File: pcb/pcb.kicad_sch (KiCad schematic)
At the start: 52 parts

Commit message: err in sch
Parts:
- removed C? (x2): 100uF, symbol Device:C_Polarized_Small
- removed D? (x3): 1N5822, Diode_THT:D_DO-201AD_P15.24mm_Horizontal, symbol Diode:1N5822
- removed R? (x2): 10k, symbol Device:R_Small
- added C?: 4.7n, symbol Device:C_Small
- added Q1: AO3400A, Package_TO_SOT_SMD:SOT-23, symbol Transistor_FET:AO3400A
- added R11, R4: 100k, symbol Device:R_Small
- added R12, R13, R14: 85, symbol Device:R_Small
- added R3: 10k, symbol Device:R_Small
- L2: renamed from L?; value . -> 1.2uH
- L3: renamed from L?; value . -> 20uH
- R2: renamed from R?; value R -> 200k
- gave numbers to parts that had none: 42
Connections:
- net +12V: now also R11.2; no longer D4.1 (K), J2.2 (Pin_2), J2.3 (Pin_3), L2.1, Q2.3 (D), Q3.3 (D), Q4.3 (D)
- net +3V3: now also R4.2
- net GND: now also Q1.2 (S); no longer J2.4 (Pin_4), Q5.3 (S)
- net at U1.5 (PB0): now also R3.2
- net at Q5.1 (G): now also Q1.3 (D), R11.1
- net at R17.2, R18.1, U4.2 (REF): now also C?.1
- net at R16.2, U3.2, U4.1 (K): now also C?.2
- new net: Q3.3 (D), R13.1
- new net: J2.3 (Pin_3), R13.2
- new net: J2.2 (Pin_2), R12.2
- new net: J2.4 (Pin_4), R14.2
- new net: D4.1 (K), L2.1, Q5.3 (S)
- new net: Q2.3 (D), R12.1
- new net: Q4.3 (D), R14.1
- new net: Q1.1 (G), R3.1, R4.1
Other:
- moved on the sheet: C6, J2, Q2, Q3, Q4, Q5, R10, R15, R17, R18, R5, R6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

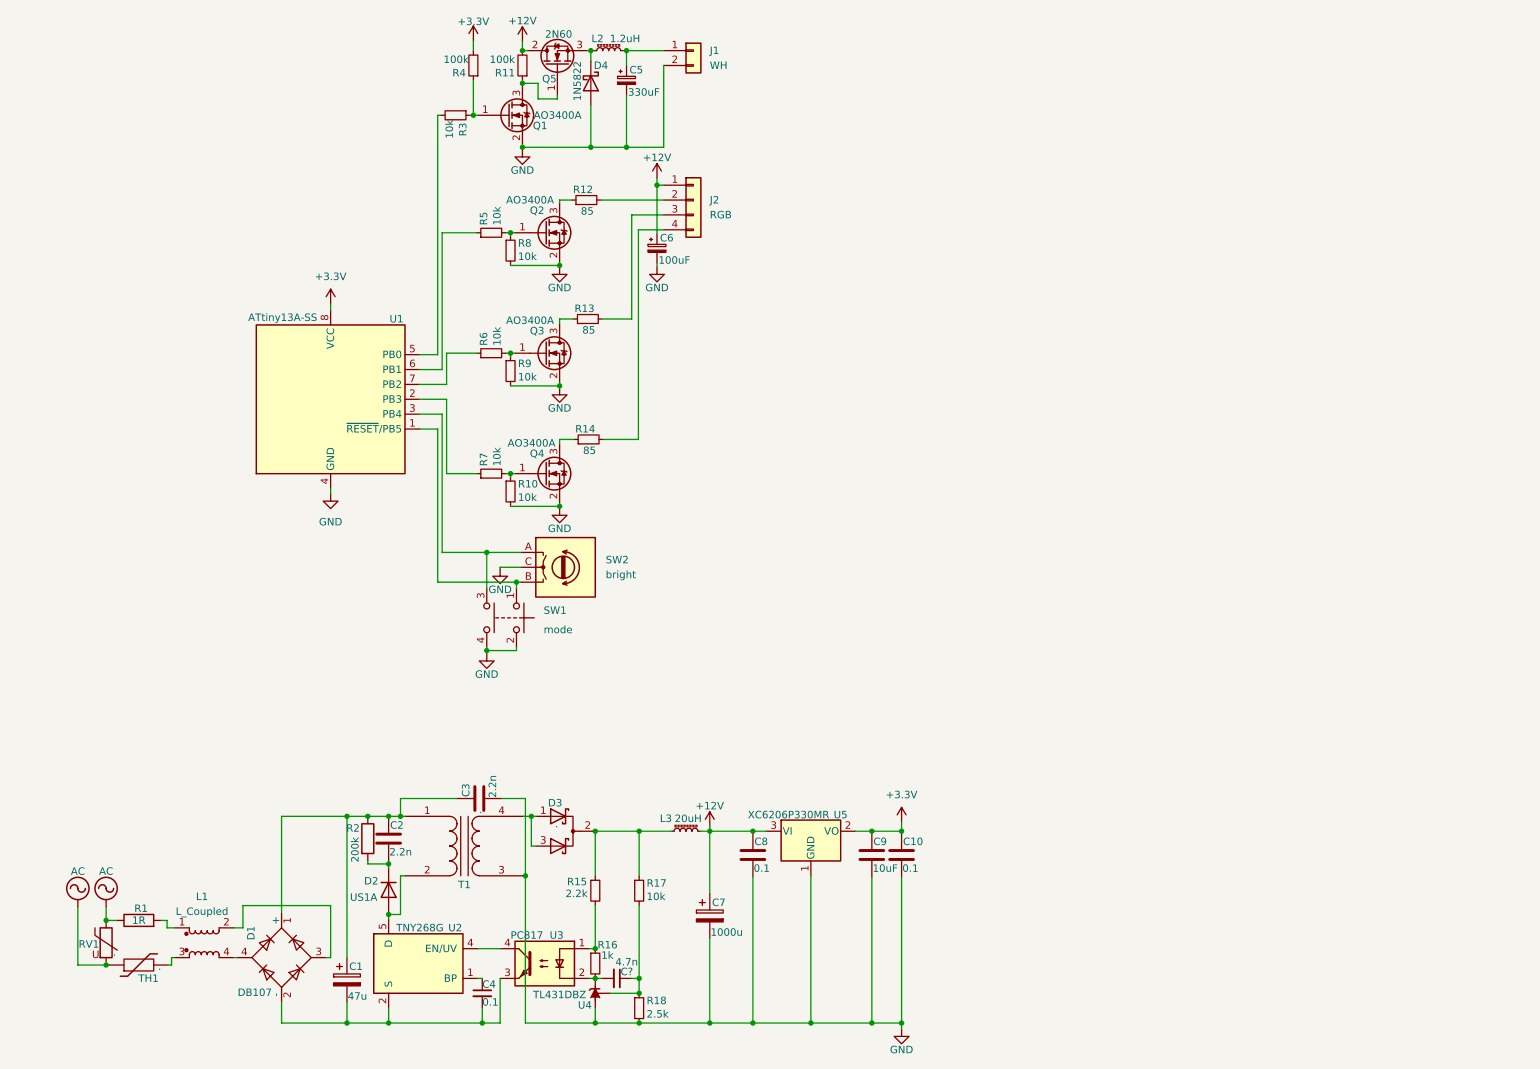
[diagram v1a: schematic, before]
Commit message: short circuit protection
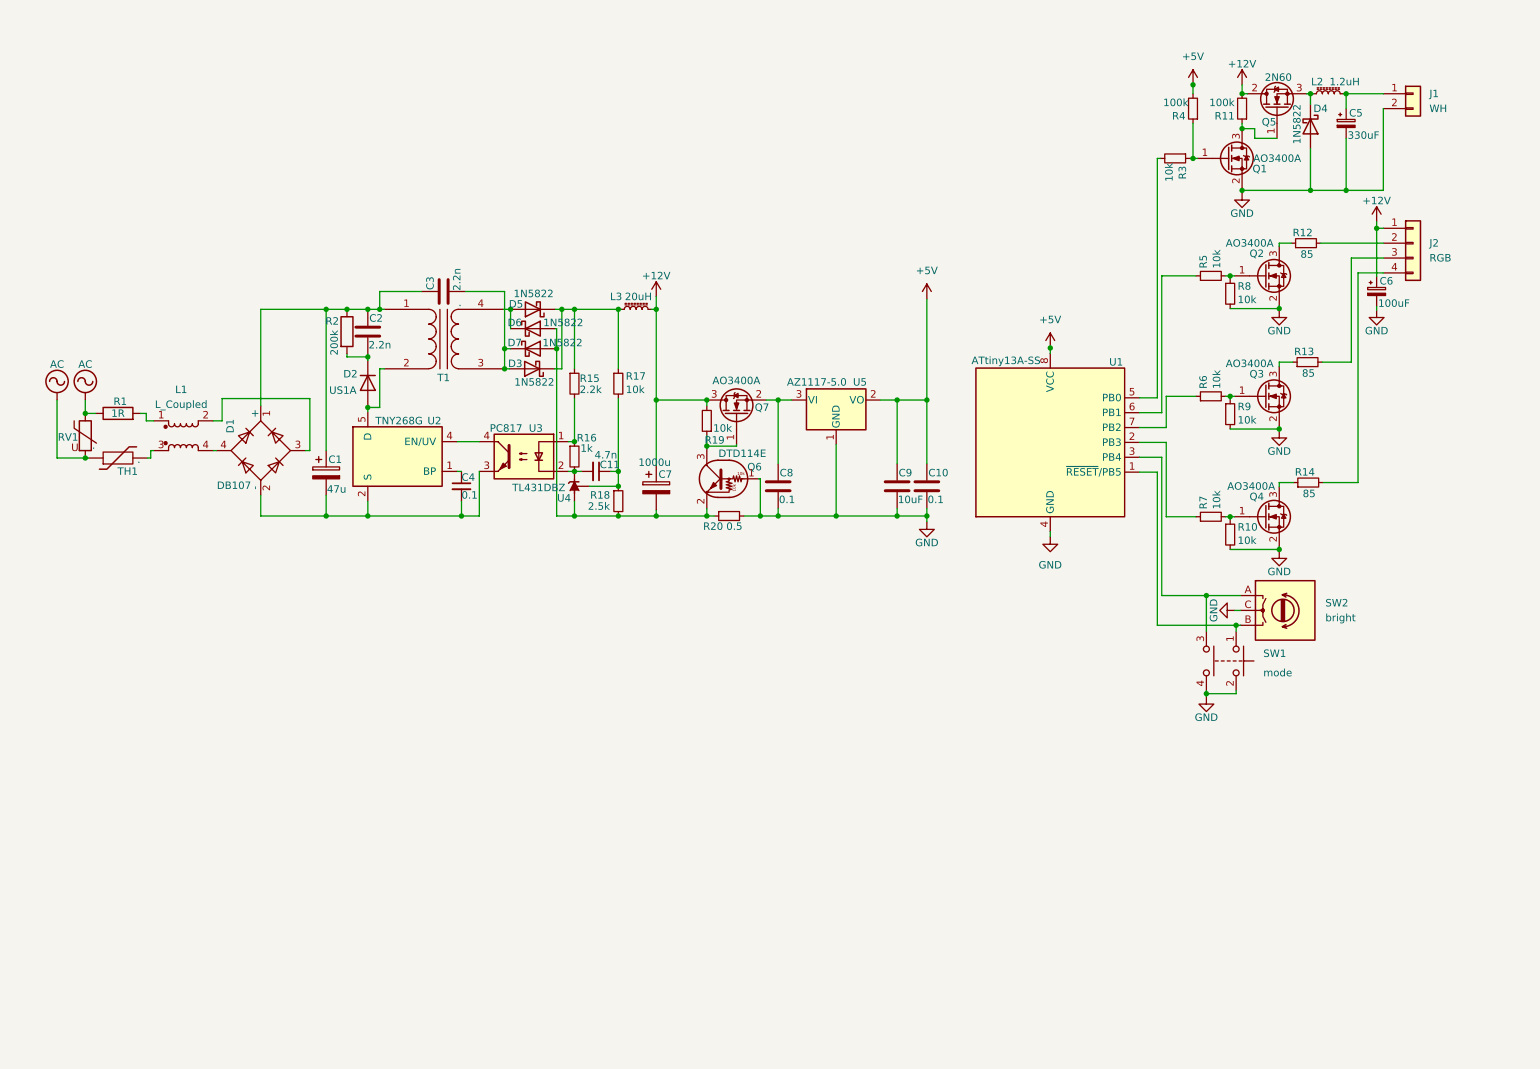
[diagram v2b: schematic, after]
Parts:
- removed D3: ., symbol Device:D_Schottky_Dual_CommonCathode_AKA_Parallel
- removed U5: XC6206P330MR, Package_TO_SOT_SMD:SOT-23, symbol Regulator_Linear:XC6206PxxxMR
- added D3, D5, D6, D7: 1N5822, Diode_THT:D_DO-201AD_P15.24mm_Horizontal, symbol Diode:1N5822
- added Q6: DTD114E, symbol Transistor_BJT:DTD114E
- added Q7: AO3400A, Package_TO_SOT_SMD:SOT-23, symbol Transistor_FET:AO3400A
- added R19: 10k, symbol Device:R_Small
- added R20: 0.5, symbol Device:R_Small
- added U5: AZ1117-5.0, symbol Regulator_Linear:AZ1117-5.0
- C1, C2, C3: footprint (none) -> Capacitor_THT:C_Axial_L3.8mm_D2.6mm_P7.50mm_Horizontal
- C4: footprint (none) -> Capacitor_SMD:C_0805_2012Metric
- gave numbers to parts that had none: 1
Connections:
- net +12V: now also Q7.3 (D), R19.2; no longer C8.1
- net GND: now also Q6.1 (B), R20.2, U5.1 (GND); no longer C3.2, C7.2, R18.2, T1.3 (SA), U4.3 (A)
- net at T1.4 (SB): now also D5.2 (A), D6.1 (K)
- net at L3.1, R15.1, R17.1: now also D3.1 (K), D5.1 (K)
- net +3V3 renamed +5V
- net +5V: now also U5.2 (VO)
- new net: C7.2, D6.2 (A), D7.2 (A), Q6.2 (E), R18.2, R20.1, U4.3 (A)
- new net: C8.1, Q7.2 (S), U5.3 (VI)
- new net: C3.2, D3.2 (A), D7.1 (K), T1.3 (SA)
- new net: Q6.3 (C), Q7.1 (G), R19.1
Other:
- moved on the sheet: C1, C10, C11, C2, C3, C4, C5, C6, C7, C8, C9, D1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

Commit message: pcb fottprints ok, layout tomorrow
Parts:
- added C12, C13, C14: 10uF, Capacitor_SMD:C_0805_2012Metric, symbol Device:C
- added J3: 220, Connector_Wire:SolderWire-0.1sqmm_1x02_P3.6mm_D0.4mm_OD1mm, symbol Connector_Generic:Conn_01x02
- C10, C8: footprint (none) -> Capacitor_SMD:C_0402_1005Metric
- C11, C9: footprint (none) -> Capacitor_SMD:C_0805_2012Metric
- C5, C7: footprint (none) -> Capacitor_THT:CP_Radial_D10.0mm_P5.00mm
- C6: footprint (none) -> Capacitor_SMD:CP_Elec_6.3x7.7
- D3, D4, D5, D6, D7: footprint Diode_THT:D_DO-201AD_P15.24mm_Horizontal -> Diode_SMD:D_SMA
- J1: footprint (none) -> Connector_PinHeader_2.54mm:PinHeader_1x02_P2.54mm_Vertical
- J2: footprint (none) -> Connector_PinHeader_2.54mm:PinHeader_1x04_P2.54mm_Vertical
- L1: footprint (none) -> Inductor_THT:Choke_Schaffner_RN212-04-12.5x18.0mm
- L2: footprint (none) -> Inductor_THT:L_Radial_D12.0mm_P10.00mm_Neosid_SD12k_style1
- L3: footprint (none) -> Inductor_THT:L_Radial_D16.8mm_P11.43mm_Vishay_IHB-1
- Q6: footprint (none) -> Package_TO_SOT_SMD:SOT-23
- R1, R2, R20: footprint (none) -> Resistor_SMD:R_1210_3225Metric
- R10, R11, R16, R17, R19, R3, R4, R5, R6, R7, R8, R9: footprint (none) -> Resistor_SMD:R_0402_1005Metric
- R12, R13, R14: footprint (none) -> Resistor_SMD:R_1206_3216Metric
- R15, R18: footprint (none) -> Resistor_SMD:R_0805_2012Metric
- RV1, TH1: footprint (none) -> Varistor:RV_Disc_D12mm_W3.9mm_P7.5mm
- SW1: footprint (none) -> Button_Switch_THT:SW_PUSH_6mm
- SW2: footprint (none) -> local:mouse_encoder
- U3: footprint Package_DIP:DIP-4_W7.62mm -> Package_SO:SOP-4_3.8x4.1mm_P2.54mm
- U5: footprint (none) -> Package_TO_SOT_SMD:SOT-223
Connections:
- net +12V: now also C12.1, C13.1, C14.2
- net at J2.3 (Pin_3), R13.2: now also C12.2
- net at J2.2 (Pin_2), R12.2: now also C14.1
- net at J2.4 (Pin_4), R14.2: now also C13.2
- net at SW1.3, SW2.A: now also U1.2 (PB3); no longer U1.3 (PB4)
- net at R7.1: now also U1.3 (PB4); no longer U1.2 (PB3)
- net AC: no longer names the net of R1.1, RV1.1
- net AC: now also J3.2 (Pin_2); no longer RV1.2, TH1.1
- new net: J3.1 (Pin_1), RV1.2, TH1.1

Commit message: pcb ok, code is coming
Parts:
- removed Q5: 2N60, Package_TO_SOT_THT:TO-220-3_Vertical, symbol Transistor_FET:IRF740
- added Q5: AOD452, Package_TO_SOT_SMD:TO-252-2, symbol Transistor_FET:QM6006D
- C1: footprint Capacitor_THT:C_Axial_L3.8mm_D2.6mm_P7.50mm_Horizontal -> Capacitor_THT:CP_Radial_D13.0mm_P7.50mm
- C11: footprint Capacitor_SMD:C_0805_2012Metric -> Capacitor_SMD:C_0402_1005Metric
- R15: footprint Resistor_SMD:R_0805_2012Metric -> Resistor_SMD:R_0402_1005Metric
- SW1: footprint Button_Switch_THT:SW_PUSH_6mm -> local:SW_PUSH_6mm_2cont
- T1: footprint (none) -> local:Transformer_NF_ETAL_P1165
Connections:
- net +12V: now also Q5.2 (D)
- net GND: now also C7.2
- net at Q1.3 (D), R11.1: now also Q5.1 (G)
- net at D6.2 (A), D7.2 (A), Q6.2 (E)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: no longer C7.2
- net at J3.2 (Pin_2), RV1.1: now also TH1.1; no longer R1.1
- net at J3.1 (Pin_1), RV1.2: now also R1.1; no longer TH1.1
- net at D4.1 (K), L2.1: now also Q5.3 (S)
- net at SW1.1, SW2.B: now also U1.3 (PB4); no longer U1.1 (~{RESET}/PB5)
- net at R6.1: now also U1.6 (PB1); no longer U1.7 (PB2)
- net at D1.3: now also L1.4; no longer L1.2
- net at D1.4: now also L1.2; no longer L1.4
- net at TH1.2: now also L1.1; no longer L1.3
- net at R5.1: now also U1.7 (PB2); no longer U1.6 (PB1)
- net at R3.2: now also U1.1 (~{RESET}/PB5); no longer U1.5 (PB0)
- net at R7.1: now also U1.5 (PB0); no longer U1.3 (PB4)
- net at R1.2: now also L1.3; no longer L1.1
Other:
- moved on the sheet: C7, J3, L1, Q6, Q7, R1, R19, R20, RV1, TH1

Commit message: operate led
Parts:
- added D8: pwr_ok, LED_SMD:LED_0603_1608Metric, symbol Device:LED
- added R21: 1k, Resistor_SMD:R_0402_1005Metric, symbol Device:R_Small
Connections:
- net +12V: now also R21.1
- net GND: now also D8.1 (K)
- new net: D8.2 (A), R21.2
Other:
- moved on the sheet: C1, C10, C11, C12, C13, C14, C2, C3, C4, C5, C6, C7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

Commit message: err in sch, some code added
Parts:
- added R22, R23, R24, R25: 10k, Resistor_SMD:R_0402_1005Metric, symbol Device:R_Small
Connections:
- net +5V: now also R22.1
- net GND: now also R24.2, R25.2; no longer SW2.C
- net at Q2.1 (G), R8.1: no longer R5.2
- net at SW1.3, U1.2 (PB3): now also SW1.1; no longer SW2.A
- new net: R22.2, R23.1, SW2.A, U1.3 (PB4)
- new net: R23.2, R24.1, SW2.B
- new net: R25.1, SW2.C
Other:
- moved on the sheet: C1, C10, C11, C12, C13, C14, C2, C3, C4, C5, C6, C7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

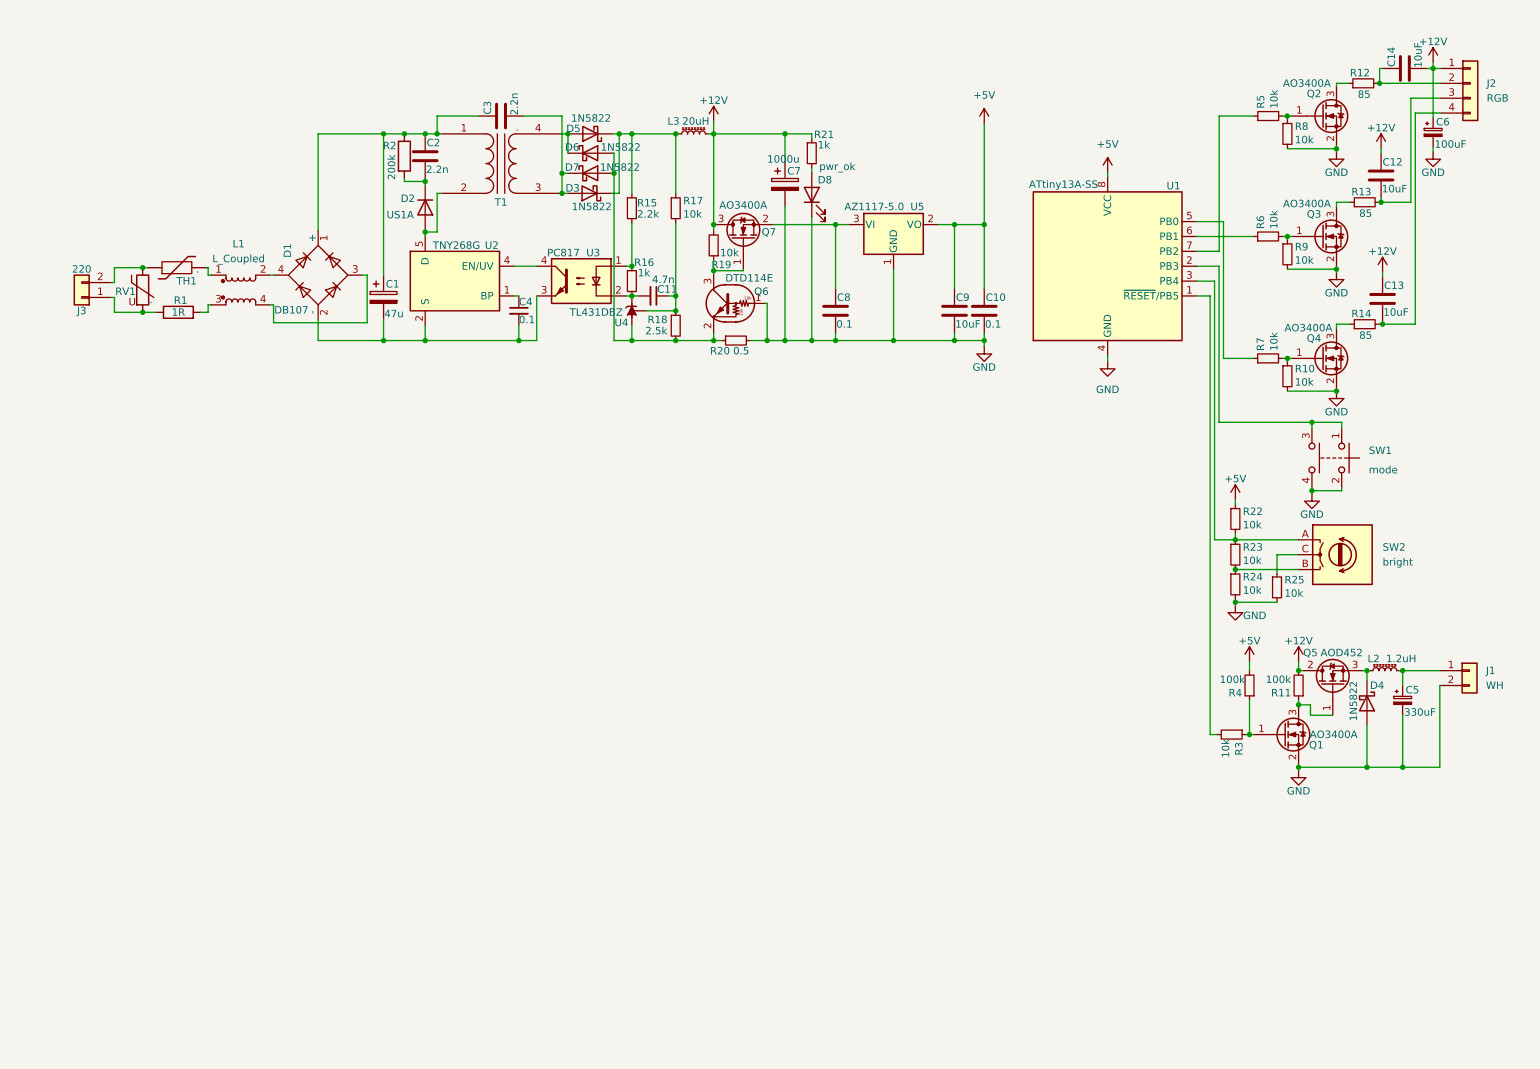
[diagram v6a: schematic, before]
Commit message: lamp on sch
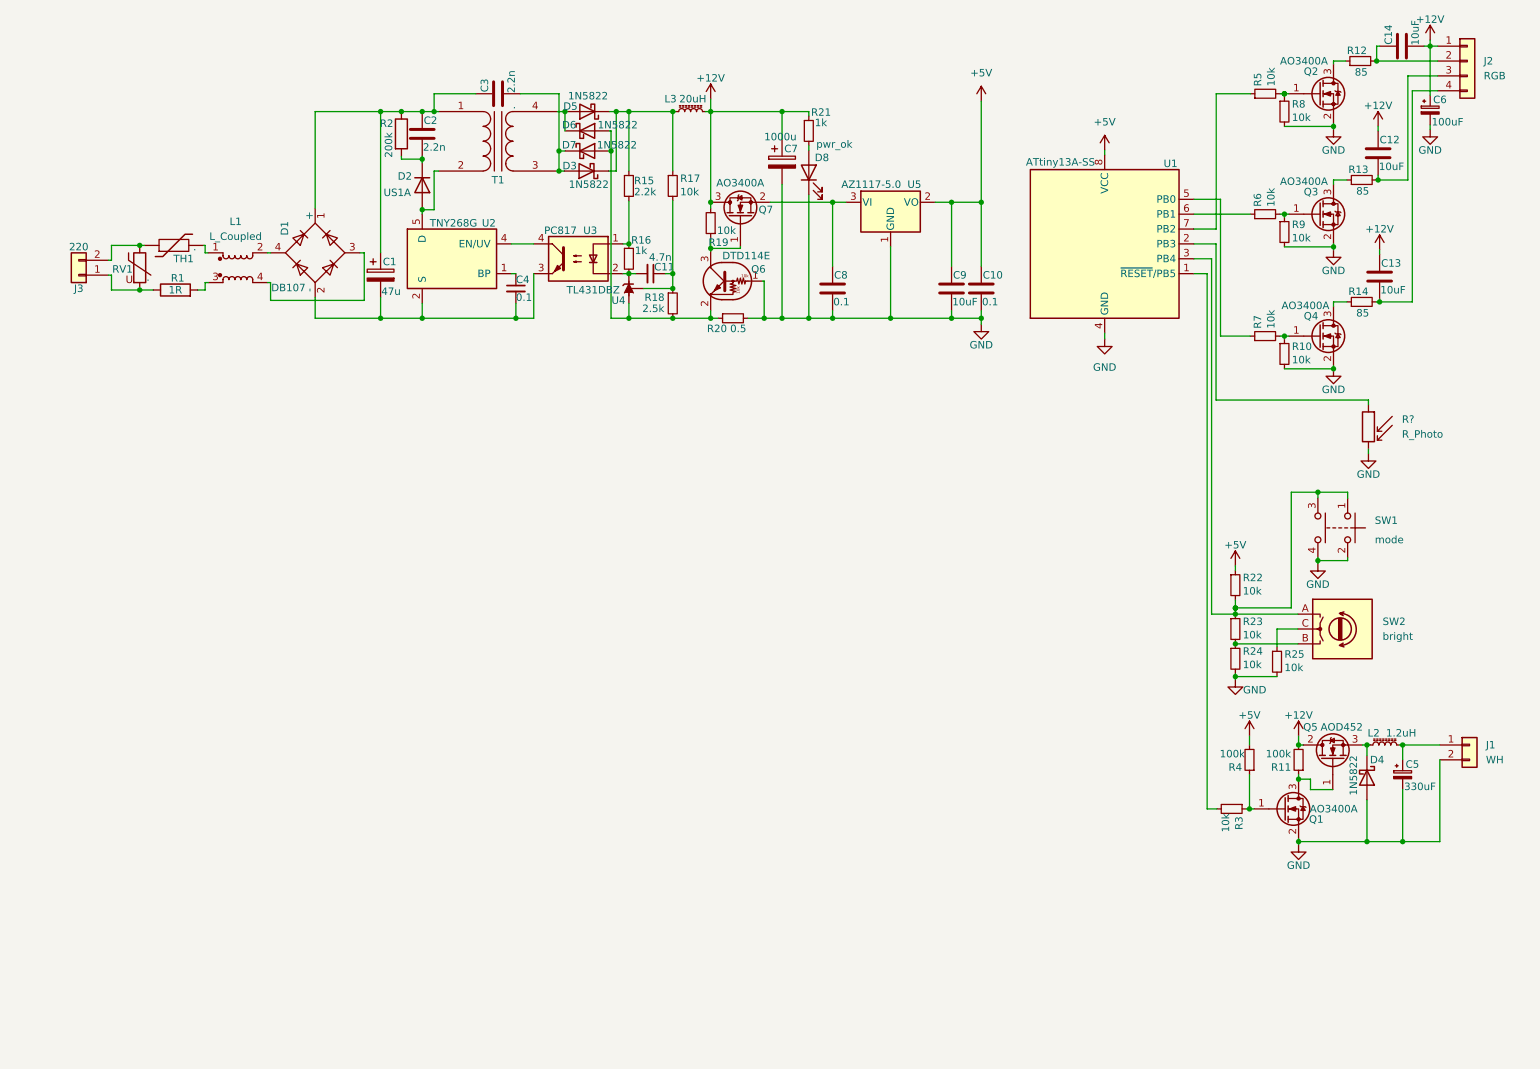
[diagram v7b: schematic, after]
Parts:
- added R?: R_Photo, symbol Device:R_Photo
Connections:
- net GND: now also R?.2
- net at R22.2, R23.1, SW2.A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: now also SW1.1, SW1.3
- new net: R?.1, U1.2 (PB3)
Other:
- moved on the sheet: C1, C10, C11, C12, C13, C14, C2, C3, C4, C5, C6, C7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
